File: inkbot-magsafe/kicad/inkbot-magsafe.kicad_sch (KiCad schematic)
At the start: 49 parts, among them J1 Panel FPC, U1 nRF52833-QDAA, U3 TPS22810DRV, U4 MIC5504-3.3, U5 BQ51050BRHL, Y1 32.768kHz, Y2 32MHz

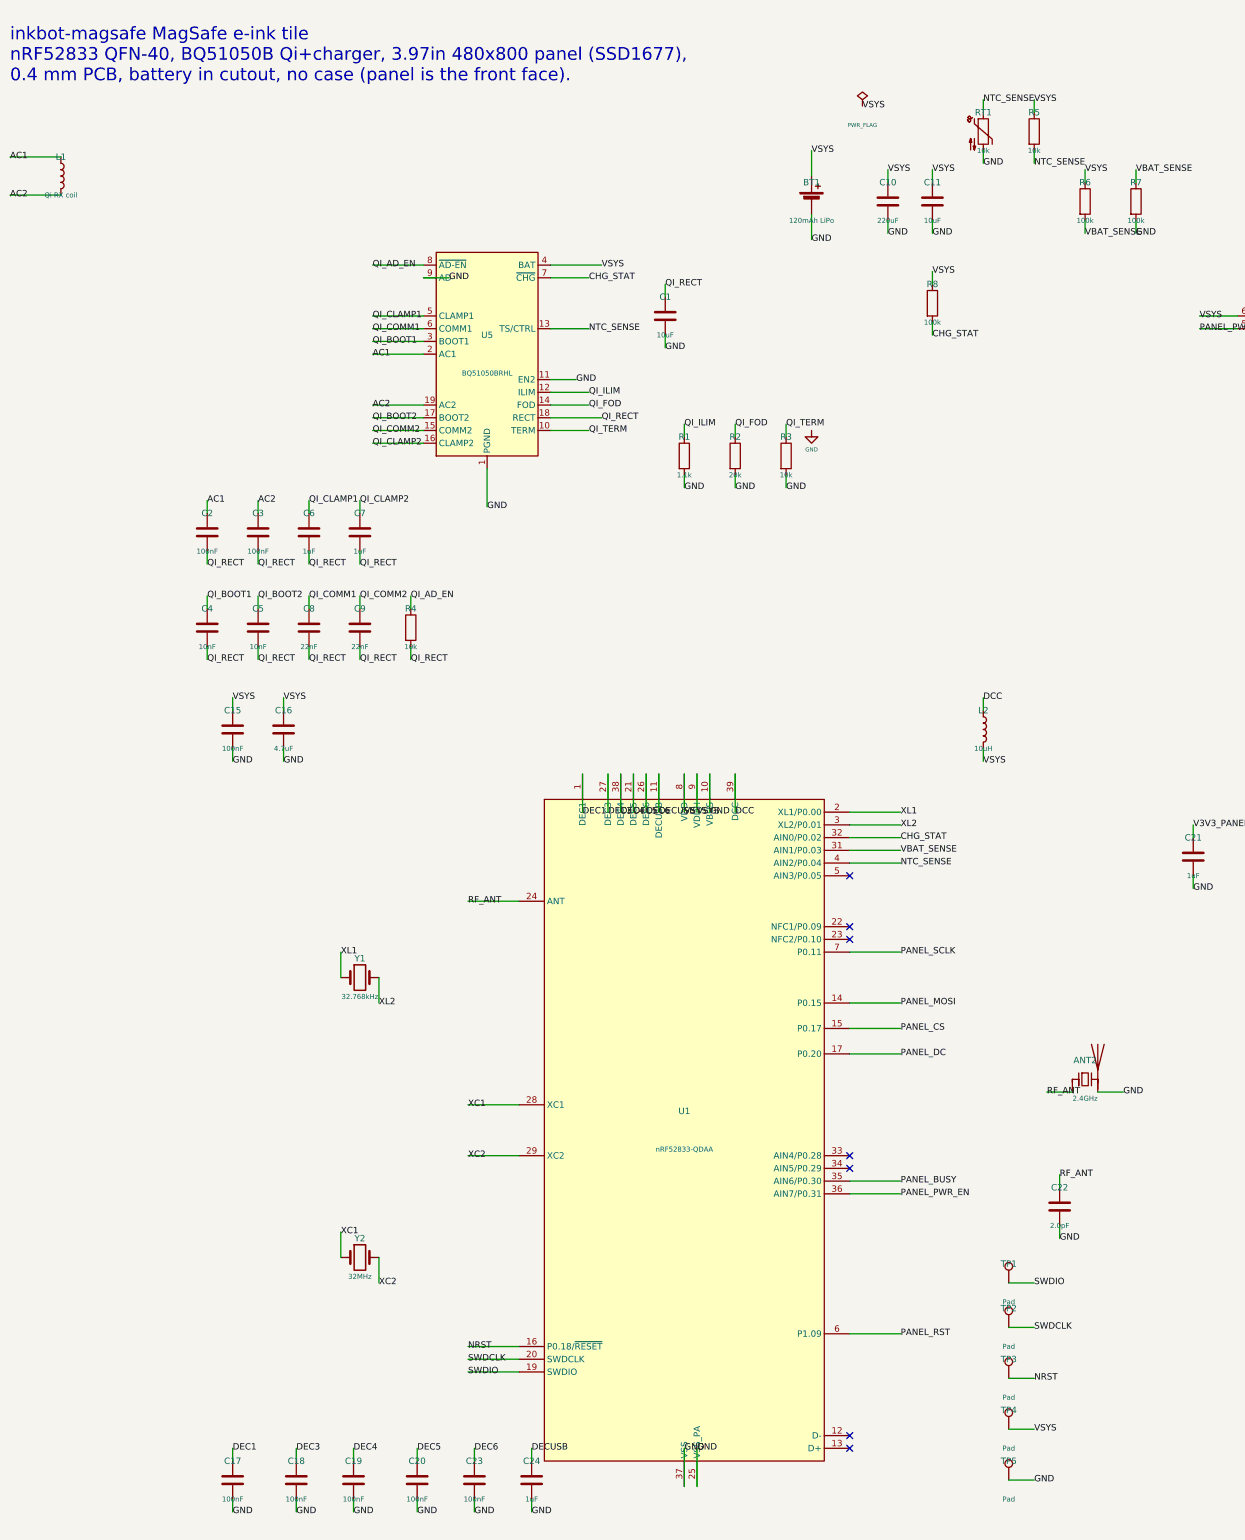
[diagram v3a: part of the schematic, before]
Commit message: inkbot-magsafe: switch to pre-certified Raytac MDBT50Q-512K module
Replace the bare nRF52833 QFN with the Raytac MDBT50Q-512K module (same
nRF52833 core, so firmware/memory are unchanged). The module integrates
the 2.4 GHz antenna, 32 MHz crystal, DC/DC, and RF match and carries
modular FCC/IC/CE/MIC/KC/SRRC approval, so the board drops the discrete
antenna, matching network, HFXO crystal, and DEC decoupling — deleting
the whole radio-layout and intentional-radiator-cert problem for ~1 mm
of added thickness (accepted).

Schematic regenerated on the module footprint (RF_Module:Raytac_MDBT50Q),
pins mapped by module pin number, netlist verified. Prototype board bumped
to 0.8 mm 4-layer. BOM, thickness table (~3.05 mm at the module), COGS
(~$34), pinmap, netlist, stackup, and design rationale updated.

Co-authored-by: Jason Hall <imjasonh@users.noreply.github.com>
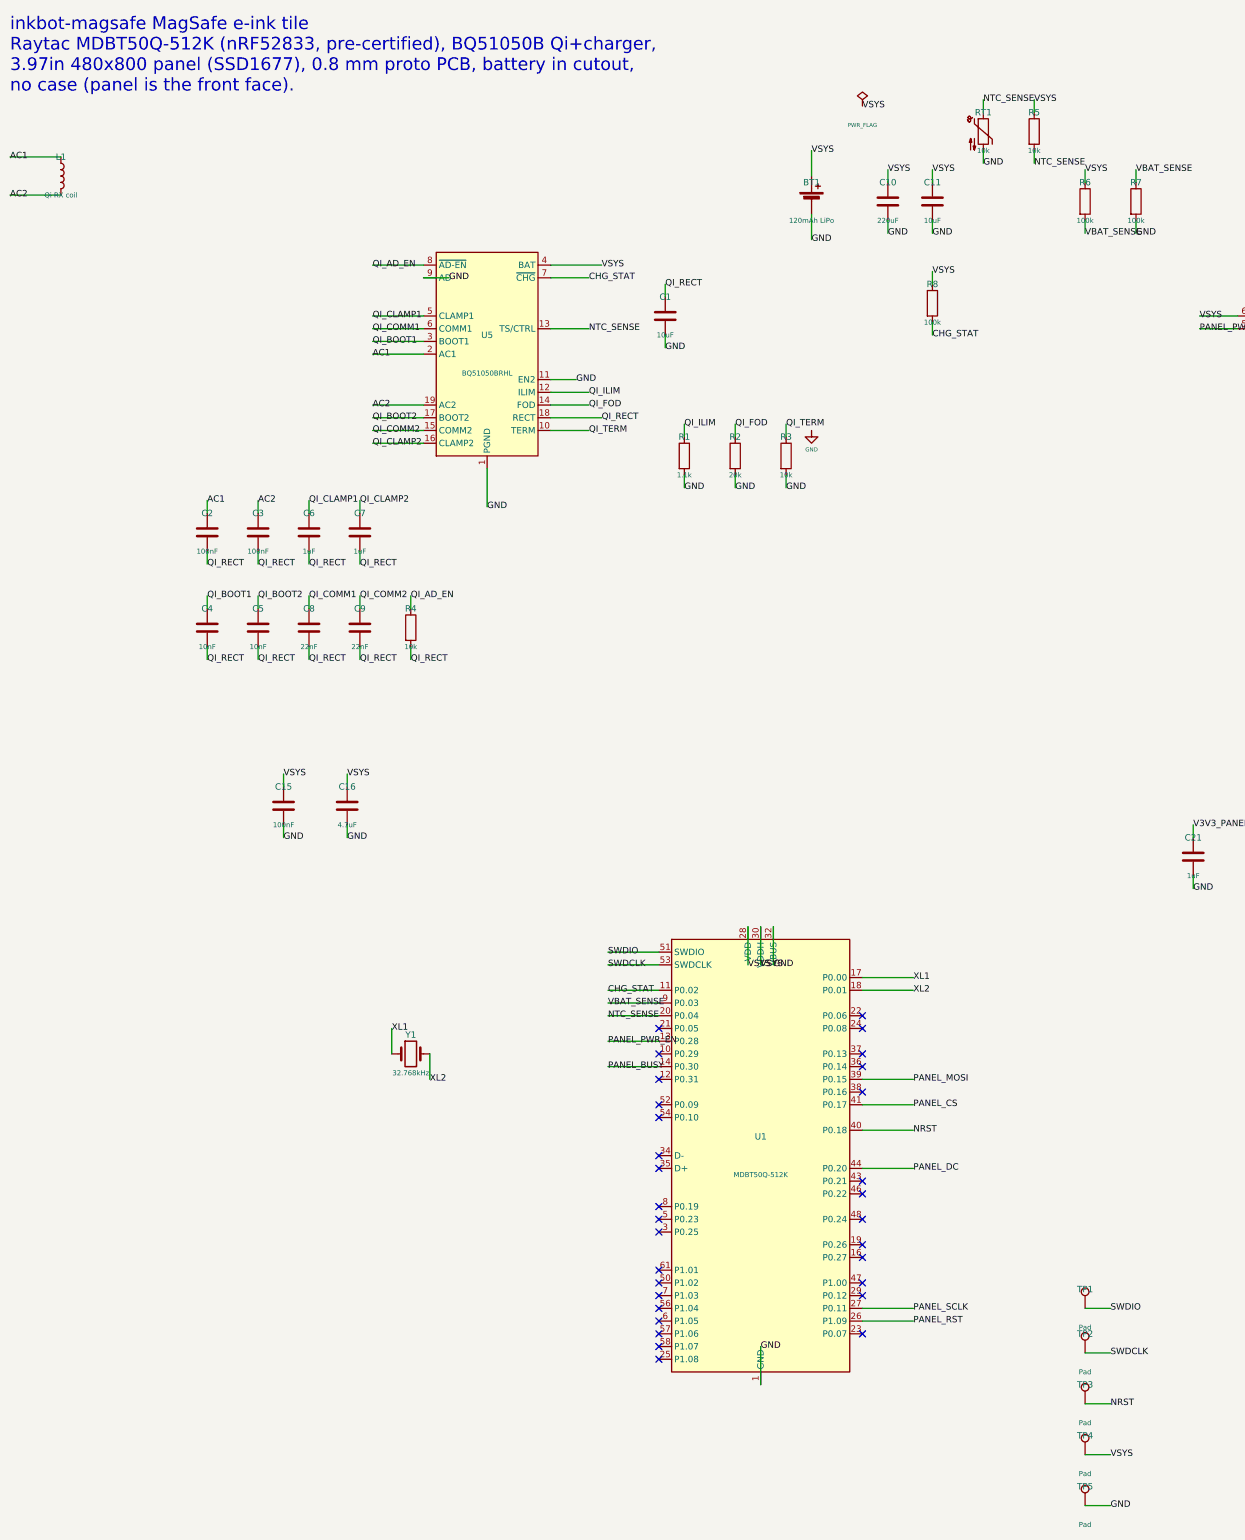
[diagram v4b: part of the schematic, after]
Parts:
- removed ANT2: 2.4GHz, Antenna_SMD:Antenna_Abracon_ACA-107-T, symbol Device:Antenna_Chip
- removed C17, C18, C19, C20, C23: 100nF, Capacitor_SMD:C_0402_1005Metric, symbol Device:C
- removed C22: 2.0pF, Capacitor_SMD:C_0402_1005Metric, symbol Device:C
- removed C24: 1uF, Capacitor_SMD:C_0402_1005Metric, symbol Device:C
- removed L2: 10uH, Inductor_SMD:L_0805_2012Metric, symbol Device:L
- removed U1: nRF52833-QDAA, Package_DFN_QFN:Nordic_QFN-40-1EP_5x5mm_P0.4mm, symbol MCU_Nordic:nRF52833_QDxx
- removed Y2: 32MHz, Crystal:Crystal_SMD_2012-2Pin_2.0x1.2mm, symbol Device:Crystal
- added U1: MDBT50Q-512K, RF_Module:Raytac_MDBT50Q, symbol RF_Module:MDBT50Q-512K
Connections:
- net CHG_STAT: now also U1.11 (P0.02)
- net GND: now also U1.1 (GND), U1.15 (GND), U1.2 (GND), U1.32 (VBUS), U1.33 (GND), U1.55 (GND)
- net NRST: now also U1.40 (P0.18)
- net NTC_SENSE: now also U1.20 (P0.04)
- net PANEL_BUSY: now also U1.14 (P0.30)
- net PANEL_CS: now also U1.41 (P0.17)
- net PANEL_DC: now also U1.44 (P0.20)
- net PANEL_MOSI: now also U1.39 (P0.15)
- net PANEL_PWR_EN: now also U1.13 (P0.28)
- net PANEL_RST: now also U1.26 (P1.09)
- net PANEL_SCLK: now also U1.27 (P0.11)
- net SWDCLK: now also U1.53 (SWDCLK)
- net SWDIO: now also U1.51 (SWDIO)
- net VBAT_SENSE: now also U1.9 (P0.03)
- net VSYS: now also U1.28 (VDD), U1.30 (VDDH)
- net XL1: now also U1.17 (P0.00)
- net XL2: now also U1.18 (P0.01)
- no-connect marks 7 -> 31
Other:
- note added: "inkbot-magsafe MagSafe e-ink tile Raytac MDBT50Q-512K (nRF52833, pre-certified), BQ51050B Qi+charger, 3.97in 480x800 panel (SSD1677), 0.8 mm proto PCB, battery in cutout, no case (panel is the front face)."
- note removed: "inkbot-magsafe MagSafe e-ink tile nRF52833 QFN-40, BQ51050B Qi+charger, 3.97in 480x800 panel (SSD1677), 0.4 mm PCB, battery in cutout, no case (panel is the front face)."

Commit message: inkbot-magsafe: regenerate the corrected electrical design
Co-authored-by: Jason Hall <imjasonh@users.noreply.github.com>
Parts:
- removed U3: TPS22810DRV, Package_TO_SOT_SMD:SOT-23-6, symbol Power_Management:TPS22810DRV
- removed U4: MIC5504-3.3, Package_TO_SOT_SMD:SOT-23-5, symbol Regulator_Linear:MIC5504-3.3YM5
- removed U5: BQ51050BRHL, Package_DFN_QFN:Texas_VQFN-RHL-20, symbol Battery_Management:BQ51050BRHL
- added C17, C19, C26, C29: 1uF 10V, Capacitor_SMD:C_0603_1608Metric, symbol Device:C
- added C18: 10uF 10V, Capacitor_SMD:C_0805_2012Metric, symbol Device:C
- added C20: 4.7nF, Capacitor_SMD:C_0603_1608Metric, symbol Device:C
- added C22: 4.7uF 10V, Capacitor_SMD:C_0603_1608Metric, symbol Device:C
- added C23, C24: 21pF C0G, Capacitor_SMD:C_0603_1608Metric, symbol Device:C
- added C25: 10nF, Capacitor_SMD:C_0603_1608Metric, symbol Device:C
- added C27, C28: 4.7uF 10V, Capacitor_SMD:C_0805_2012Metric, symbol Device:C
- added C30: 1uF 6.3V, Capacitor_SMD:C_0603_1608Metric, symbol Device:C
- added C31, C32, C33, C34, C35, C37: 4.7uF 25V, Capacitor_SMD:C_0805_2012Metric, symbol Device:C
- added C36: 1uF 50V, Capacitor_SMD:C_0603_1608Metric, symbol Device:C
- added D1, D2, D3: MBR0530, Diode_SMD:D_SOD-123, symbol Device:D
- added J2: Protected battery + NTC, Connector_Molex:Molex_Pico-EZmate_78171-0003_1x03-1MP_P1.20mm_Vertical, symbol Connector_Generic:Conn_01x03
- added J3: WR222230-26M8-G coil, Connector_Wire:SolderWire-0.5sqmm_1x02_P4.8mm_D0.9mm_OD2.3mm_Relief2x, symbol Connector_Generic:Conn_01x02
- added L2: WR222230-26M8-G 27uH, symbol Device:L
- added Q1: Si1308EDL-T1-GE3, Package_TO_SOT_SMD:SOT-323_SC-70, symbol Device:Q_NMOS_GSD
- added R10: 330k 1%, Resistor_SMD:R_0603_1608Metric, symbol Device:R
- added R11: 2.2R 1%, Resistor_SMD:R_0603_1608Metric, symbol Device:R
- added R12, R13, R14: 1M, Resistor_SMD:R_0603_1608Metric, symbol Device:R
- added R9: 1M 1%, Resistor_SMD:R_0603_1608Metric, symbol Device:R
- added RT2: 10k 3435K coil NTC, Resistor_SMD:R_0402_1005Metric, symbol Device:Thermistor_NTC
- added TP6: SYS, TestPoint:TestPoint_Pad_D1.0mm, symbol Connector:TestPoint
- added TP7: BAT, TestPoint:TestPoint_Pad_D1.0mm, symbol Connector:TestPoint
- added TP8: QI_OUT, TestPoint:TestPoint_Pad_D1.0mm, symbol Connector:TestPoint
- added TP9: PANEL_3V0, TestPoint:TestPoint_Pad_D1.0mm, symbol Connector:TestPoint
- added U2: BQ51013C, Package_DFN_QFN:Texas_VQFN-RHL-20, symbol inkbot_magsafe:BQ51013C
- added U3: BQ25185DLHR, inkbot_magsafe:BQ25185_DLH0010A, symbol inkbot_magsafe:BQ25185
- added U4: TPS7A2030PDBVR, Package_TO_SOT_SMD:SOT-23-5, symbol inkbot_magsafe:TPS7A2030P
- BT1: value 120mAh LiPo -> LP252030 100mAh protected
- C1: value 10uF -> 33nF 50V
- C10: value 220uF -> 22nF 50V; footprint Capacitor_SMD:C_1206_3216Metric -> Capacitor_SMD:C_0603_1608Metric
- C11: value 10uF -> 22nF 50V
- C12: value 1nF -> 10uF 25V; footprint Capacitor_SMD:C_0402_1005Metric -> Capacitor_SMD:C_0805_2012Metric
- C13: value 1uF -> 10uF 25V; footprint Capacitor_SMD:C_0402_1005Metric -> Capacitor_SMD:C_0805_2012Metric
- C14: value 1uF -> 100nF 50V; footprint Capacitor_SMD:C_0402_1005Metric -> Capacitor_SMD:C_0603_1608Metric
- C15: value 100nF -> 10uF 10V; footprint Capacitor_SMD:C_0402_1005Metric -> Capacitor_SMD:C_0805_2012Metric
- C16: value 4.7uF -> 100nF 10V
- C2: value 100nF -> 33nF 50V; footprint Capacitor_SMD:C_0402_1005Metric -> Capacitor_SMD:C_0603_1608Metric
- C21: value 1uF -> 4.7uF 10V
- C3: value 100nF -> 15nF 50V; footprint Capacitor_SMD:C_0402_1005Metric -> Capacitor_SMD:C_0603_1608Metric
- C4: value 10nF -> 820pF C0G 50V; footprint Capacitor_SMD:C_0402_1005Metric -> Capacitor_SMD:C_0603_1608Metric
- C5: value 10nF -> 130pF C0G 50V; footprint Capacitor_SMD:C_0402_1005Metric -> Capacitor_SMD:C_0603_1608Metric
- C6, C7: value 1uF -> 10nF 50V; footprint Capacitor_SMD:C_0402_1005Metric -> Capacitor_SMD:C_0603_1608Metric
- C8, C9: value 22nF -> 470nF 25V; footprint Capacitor_SMD:C_0402_1005Metric -> Capacitor_SMD:C_0603_1608Metric
- J1: value Panel FPC -> GDEM0397T81P panel FPC
- L1: value Qi RX coil -> VLS252010CX-100M-1 10uH; footprint Inductor_SMD:L_1210_3225Metric -> Inductor_SMD:L_TDK_NLV25_2.5x2.0mm
- R1: value 1.1k -> 845R 1%; footprint Resistor_SMD:R_0402_1005Metric -> Resistor_SMD:R_0603_1608Metric
- R2: value 20k -> 200R 1%; footprint Resistor_SMD:R_0402_1005Metric -> Resistor_SMD:R_0603_1608Metric
- R3: value 10k -> 20k 1%; footprint Resistor_SMD:R_0402_1005Metric -> Resistor_SMD:R_0603_1608Metric
- R4: value 10k -> DNP; footprint Resistor_SMD:R_0402_1005Metric -> Resistor_SMD:R_0603_1608Metric
- R5: value 10k -> 100k; footprint Resistor_SMD:R_0402_1005Metric -> Resistor_SMD:R_0603_1608Metric
- R6: value 100k -> 24k 1%; footprint Resistor_SMD:R_0402_1005Metric -> Resistor_SMD:R_0603_1608Metric
- R7: value 100k -> 7.5k 1%; footprint Resistor_SMD:R_0402_1005Metric -> Resistor_SMD:R_0603_1608Metric
- R8: value 100k -> 2k; footprint Resistor_SMD:R_0402_1005Metric -> Resistor_SMD:R_0603_1608Metric
- RT1: value 10k -> 10k 3435K bonded to cell; footprint Resistor_SMD:R_0402_1005Metric -> (none)
- TP1: value Pad -> SWDIO; footprint TestPoint:TestPoint_Pad_D1.5mm -> TestPoint:TestPoint_Pad_D1.0mm
- TP2: value Pad -> SWDCLK; footprint TestPoint:TestPoint_Pad_D1.5mm -> TestPoint:TestPoint_Pad_D1.0mm
- TP3: value Pad -> NRST; footprint TestPoint:TestPoint_Pad_D1.5mm -> TestPoint:TestPoint_Pad_D1.0mm
- TP4: value Pad -> VDD_NRF; footprint TestPoint:TestPoint_Pad_D1.5mm -> TestPoint:TestPoint_Pad_D1.0mm
- TP5: value Pad -> GND; footprint TestPoint:TestPoint_Pad_D1.5mm -> TestPoint:TestPoint_Pad_D1.0mm
- Y1: value 32.768kHz -> FC-135 32.768kHz 12.5pF; footprint Crystal:Crystal_SMD_2012-2Pin_2.0x1.2mm -> Crystal:Crystal_SMD_3215-2Pin_3.2x1.5mm
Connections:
- net PANEL_CT is gone; now on net QI_RECT: C12.1
- net QI_TERM is gone; now on net QI_RECT: R3.1
- net VSW_PANEL is gone; now on net QI_RECT: C13.1
- net PANEL_BUSY: now also J1.9 (Pin_9); no longer J1.5 (Pin_5)
- net PANEL_CS: now also J1.12 (Pin_12); no longer J1.8 (Pin_8)
- net PANEL_DC: now also J1.11 (Pin_11); no longer J1.7 (Pin_7)
- net PANEL_MOSI: now also J1.14 (Pin_14); no longer J1.10 (Pin_10)
- net PANEL_PWR_EN: now also U1.12 (P0.31), U4.3 (EN); no longer U1.13 (P0.28)
- net PANEL_RST: now also J1.10 (Pin_10); no longer J1.6 (Pin_6)
- net PANEL_SCLK: now also J1.13 (Pin_13); no longer J1.9 (Pin_9)
- net QI_BOOT1: now also C6.1, U2.3 (BOOT1); no longer C4.1
- net QI_BOOT2: now also C7.1, U2.17 (BOOT2); no longer C5.1
- net QI_CLAMP1: now also C8.1, U2.5 (CLAMP1); no longer C6.1
- net QI_CLAMP2: now also C9.1, U2.16 (CLAMP2); no longer C7.1
- net QI_COMM1: now also C10.1, U2.6 (COMM1); no longer C8.1
- net QI_COMM2: now also C11.1, U2.15 (COMM2); no longer C9.1
- net QI_FOD: now also R1.2, R3.2, R4.2, U2.14 (FOD)
- net QI_ILIM: now also U2.12 (ILIM)
- net QI_RECT: now also C14.1, U2.18 (RECT); no longer C1.1, C2.2, C3.2, C4.2, C5.2, C6.2, C7.2, C8.2, C9.2, R4.2
- net VBAT_SENSE: now also C25.1, R10.1, R9.2; no longer R6.2, R7.1
- net XL1: now also C23.1
- net XL2: now also C24.1
- net CHG_STAT2: now reaches U1.21 (P0.05)
- net CHG_STAT2: now also U3.3 (STAT2)
- net CHG_EN_N: now reaches U1.22 (P0.06)
- net CHG_EN_N: now also R5.1, U3.4 (~{CE})
- net PANEL_3V0: now reaches J1.15 (Pin_15)
- net PANEL_3V0: now also J1.16 (Pin_16), L1.1, C27.1, C28.1, C29.1, TP9.1, U4.5 (OUT)
- net EP: now reaches J1.17 (Pin_17)
- net EP: now also BT1.2 (-), C12.2, C13.2, C14.2, C15.2, C16.2, C21.2, J1.8 (Pin_8), R2.2, R5.2, R6.2, R7.2, RT1.2, TP5.1, U1.1 (GND), U1.15 (GND), U1.2 (GND), U1.33 (GND), U1.55 (GND), C17.2, C18.2, C19.2, C20.2, C22.2, C23.2, C24.2, C25.2, C26.2, C27.2, C28.2, C29.2, C30.2, C31.2, C32.2, C33.2, C34.2, C35.2, C36.2, D2.1 (K), J2.3 (Pin_3), R10.2, R11.2, R12.2, R13.2, R14.2, RT2.2, U2.1 (PGND), U2.10 (EN1), U2.11 (EN2), U2.20 (PGND), U2.21 (EP), U2.9 (AD), U3.11 (EP), U3.5 (GND), U4.2 (GND)
- net PANEL_VDD: now reaches J1.18 (Pin_18)
- net PANEL_VDD: now also C30.1
- net PANEL_VSH1: now reaches J1.20 (Pin_20)
- net PANEL_VSH1: now also C32.1
- net PANEL_VGH: now reaches J1.21 (Pin_21)
- net PANEL_VGH: now also C33.1, D3.1 (K), R13.1
- net PANEL_VSL: now reaches J1.22 (Pin_22)
- net PANEL_VSL: now also C34.1
- net PANEL_VGL: now reaches J1.23 (Pin_23)
- net PANEL_VGL: now also C35.1, D1.2 (A), R14.1
- net PANEL_VCOM: now reaches J1.24 (Pin_24)
- net PANEL_VCOM: now also C36.1
- net AC1 renamed QI_COIL_A
- net QI_COIL_A: now also C1.1, C3.1, J3.1 (Pin_1), L2.1; no longer L1.1
- net AC2 renamed PANEL_SW
- net PANEL_SW: now also C37.1, D3.2 (A), Q1.3 (D); no longer C3.1
- net CHG_STAT renamed CHG_ISET_COMP
- net CHG_ISET_COMP: now also C20.1; no longer U1.11 (P0.02)
- removed net GND: BT1.2 (-), C1.2, C10.2, C11.2, C12.2, C13.2, C14.2, C15.2, C16.2, C21.2, J1.3 (Pin_3), J1.4 (Pin_4), R1.2, R2.2, R3.2, R7.2, RT1.2, TP5.1, U1.1 (GND), U1.15 (GND), U1.2 (GND), U1.32 (VBUS), U1.33 (GND), U1.55 (GND)
- removed net NTC_SENSE: R5.2, RT1.1, U1.20 (P0.04)
- net QI_AD_EN renamed QI_OUT
- net QI_OUT: now also C15.1, C16.1, C17.1, TP8.1, U2.4 (OUT), U3.10 (IN)
- removed net V3V3_PANEL: C14.1, C21.1, J1.1 (Pin_1), J1.2 (Pin_2)
- removed net VSYS: BT1.1 (+), C10.1, C11.1, C15.1, C16.1, R5.1, R6.1, R8.1, TP4.1, U1.28 (VDD), U1.30 (VDDH)
- new net BAT: BT1.1 (+), C19.1, J2.1 (Pin_1), R9.1, TP7.1, U3.2 (BAT)
- new net BAT_NTC: J2.2 (Pin_2), RT1.1, U3.6 (TS/MR)
- new net CHG_ISET: R7.1, R8.1, U3.8 (ISET)
- new net CHG_STAT1: U1.20 (P0.04), U3.9 (STAT1)
- new net CHG_VSET: R6.1, U3.7 (ILIM/VSET)
- new net PANEL_GDR: J1.2 (Pin_2), Q1.1 (G), R12.1
- new net PANEL_PUMP: C37.2, D1.1 (K), D2.2 (A)
- new net PANEL_RESE: J1.3 (Pin_3), Q1.2 (S), R11.1
- new net PANEL_VSH2: C31.1, J1.5 (Pin_5)
- new net QI_AC1: C1.2, C10.2, C2.2, C3.2, C4.1, C5.1, C6.2, C8.2, U2.2 (AC1)
- new net QI_AC2: C11.2, C4.2, C5.2, C7.2, C9.2, J3.2 (Pin_2), L2.2, U2.19 (AC2)
- new net QI_COIL_NTC: RT2.1, U2.13 (TS/CTRL)
- new net QI_PRESENT: U1.11 (P0.02), U2.7 (CHG)
- new net SYS: C18.1, C21.1, C26.1, TP6.1, U1.30 (VDDH), U3.1 (SYS), U4.1 (IN)
- new net VDD_NRF: C22.1, TP4.1, U1.28 (VDD)
- no-connect marks 31 -> 48
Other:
- note added: "inkbot-magsafe EVT schematic BQ51013C Qi 1.3 receiver + BQ25185 40 mA protected-cell charger, Raytac MDBT50Q-512K in VDDH mode, and the complete GDEM0397T81P SSD1677 boost circuit. Qi resonance and FOD values require EVT tuning."
- note removed: "inkbot-magsafe MagSafe e-ink tile Raytac MDBT50Q-512K (nRF52833, pre-certified), BQ51050B Qi+charger, 3.97in 480x800 panel (SSD1677), 0.8 mm proto PCB, battery in cutout, no case (panel is the front face)."

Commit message: inkbot-magsafe: update the coil connector netlist
Co-authored-by: Jason Hall <imjasonh@users.noreply.github.com>
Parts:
- J3: footprint Connector_Wire:SolderWire-0.5sqmm_1x02_P4.8mm_D0.9mm_OD2.3mm_Relief2x -> inkbot_magsafe:Coil_SolderPads

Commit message: inkbot-magsafe: harden the EVT hardware design
Co-authored-by: Jason Hall <imjasonh@users.noreply.github.com>
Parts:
- removed C25: 10nF, Capacitor_SMD:C_0603_1608Metric, symbol Device:C
- removed R10: 330k 1%, Resistor_SMD:R_0603_1608Metric, symbol Device:R
- removed R13, R14: 1M, Resistor_SMD:R_0603_1608Metric, symbol Device:R
- removed R9: 1M 1%, Resistor_SMD:R_0603_1608Metric, symbol Device:R
- added C38: 220uF 6.3V X5R, Capacitor_SMD:C_1206_3216Metric, symbol Device:C
- C1, C2, C3: footprint Capacitor_SMD:C_0603_1608Metric -> Capacitor_SMD:C_0805_2012Metric
- C12, C13: footprint Capacitor_SMD:C_0805_2012Metric -> Capacitor_SMD:C_1206_3216Metric
- C15: value 10uF 10V -> 10uF 25V; footprint Capacitor_SMD:C_0805_2012Metric -> Capacitor_SMD:C_1206_3216Metric
- C17, C29: value 1uF 10V -> 1uF 25V
- C18: value 10uF 10V -> 10uF 25V
- C23, C24: value 21pF C0G -> 22pF C0G
- C28: value 4.7uF 10V -> 4.7uF 25V
- C30: value 1uF 6.3V -> 1uF 50V
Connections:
- net EP: now also C38.2
- net SYS: now also C38.1
- net VBAT_SENSE: no longer names the net of U1.9 (P0.03)
- no-connect marks 48 -> 49

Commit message: inkbot-magsafe: bound panel inrush and sense coil heat
Co-authored-by: Jason Hall <imjasonh@users.noreply.github.com>
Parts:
- C1, C2: value 33nF 50V -> 33nF C0G 50V
- C27: value 4.7uF 10V -> 100uF 6.3V X5R; footprint Capacitor_SMD:C_0805_2012Metric -> Capacitor_SMD:C_1206_3216Metric
- C3: value 15nF 50V -> 15nF C0G 50V
- C38: value 220uF 6.3V X5R -> 47uF 10V X5R
- J3: value WR222230-26M8-G coil -> WR222230 coil + bonded NTC; symbol Connector_Generic:Conn_01x02 -> Connector_Generic:Conn_01x04
- RT2: footprint Resistor_SMD:R_0402_1005Metric -> (none)
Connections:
- net EP: now also J3.4 (Pin_4)
- net QI_COIL_NTC: now also J3.3 (Pin_3)
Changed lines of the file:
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@@
     )
   )
-  (symbol (lib_id "Connector_Generic:Conn_01x02") (at 25.40 44.45 0)
+  (symbol (lib_id "Connector_Generic:Conn_01x04") (at 25.40 44.45 0)
     (property "Reference" "J3" (at 25.40 40.64 0)
       (effects (font (size 1.27 1.27))))
-    (property "Value" "WR222230-26M8-G coil" (at 25.40 48.26 0)
+    (property "Value" "WR222230 coil + bonded NTC" (at 25.40 48.26 0)
       (effects (font (size 1.0 1.0))))
     (property "Footprint" "inkbot_magsafe:Coil_SolderPads" (at 25.40 49.53 0)
@@
     (property "Reference" "C1" (at 41.91 66.04 0)
       (effects (font (size 1.27 1.27))))
-    (property "Value" "33nF 50V" (at 41.91 73.66 0)
+    (property "Value" "33nF C0G 50V" (at 41.91 73.66 0)
       (effects (font (size 1.0 1.0))))
     (property "Footprint" "Capacitor_SMD:C_0805_2012Metric" (at 41.91 74.93 0)
@@
     (property "Reference" "C2" (at 49.53 66.04 0)
       (effects (font (size 1.27 1.27))))
-    (property "Value" "33nF 50V" (at 49.53 73.66 0)
+    (property "Value" "33nF C0G 50V" (at 49.53 73.66 0)
       (effects (font (size 1.0 1.0))))
     (property "Footprint" "Capacitor_SMD:C_0805_2012Metric" (at 49.53 74.93 0)
@@
     (property "Reference" "C3" (at 58.42 66.04 0)
       (effects (font (size 1.27 1.27))))
-    (property "Value" "15nF 50V" (at 58.42 73.66 0)
+    (property "Value" "15nF C0G 50V" (at 58.42 73.66 0)
       (effects (font (size 1.0 1.0))))
     (property "Footprint" "Capacitor_SMD:C_0805_2012Metric" (at 58.42 74.93 0)
@@
     (property "Value" "10k 3435K coil NTC" (at 165.10 68.58 0)
       (effects (font (size 1.0 1.0))))
-    (property "Footprint" "Resistor_SMD:R_0402_1005Metric" (at 165.10 69.85 0)
+    (property "Footprint" "" (at 165.10 69.85 0)
       (effects (font (size 1.27 1.27)) hide))
     (property "LCSC" "" (at 165.10 71.12 0)
@@
     (property "Reference" "C38" (at 229.87 171.45 0)
       (effects (font (size 1.27 1.27))))
-    (property "Value" "220uF 6.3V X5R" (at 229.87 179.07 0)
+    (property "Value" "47uF 10V X5R" (at 229.87 179.07 0)
       (effects (font (size 1.0 1.0))))
     (property "Footprint" "Capacitor_SMD:C_1206_3216Metric" (at 229.87 180.34 0)
@@
     (property "Reference" "C27" (at 304.80 156.21 0)
       (effects (font (size 1.27 1.27))))
-    (property "Value" "4.7uF 10V" (at 304.80 163.83 0)
-      (effects (font (size 1.0 1.0))))
-    (property "Footprint" "Capacitor_SMD:C_0805_2012Metric" (at 304.80 165.10 0)
+    (property "Value" "100uF 6.3V X5R" (at 304.80 163.83 0)
+      (effects (font (size 1.0 1.0))))
+    (property "Footprint" "Capacitor_SMD:C_1206_3216Metric" (at 304.80 165.10 0)
       (effects (font (size 1.27 1.27)) hide))
     (property "LCSC" "" (at 304.80 166.37 0)
@@
     (stroke (width 0) (type default))
   )
+  (wire (pts (xy 20.32 41.91) (xy 12.70 41.91))
+    (stroke (width 0) (type default))
+  )
   (wire (pts (xy 20.32 44.45) (xy 12.70 44.45))
     (stroke (width 0) (type default))
@@
     (stroke (width 0) (type default))
   )
+  (wire (pts (xy 20.32 49.53) (xy 12.70 49.53))
+    (stroke (width 0) (type default))
+  )
   (wire (pts (xy 25.40 21.59) (xy 25.40 16.51))
     (stroke (width 0) (type default))
@@
     (effects (font (size 1.27 1.27)) (justify left))
   )
-  (label "QI_COIL_A" (at 12.70 44.45 0)
-    (effects (font (size 1.27 1.27)) (justify left))
-  )
-  (label "QI_AC2" (at 12.70 46.99 0)
-    (effects (font (size 1.27 1.27)) (justify left))
-  )
+  (label "QI_COIL_A" (at 12.70 41.91 0)
+    (effects (font (size 1.27 1.27)) (justify left))
+  )
+  (label "QI_AC2" (at 12.70 44.45 0)
+    (effects (font (size 1.27 1.27)) (justify left))
+  )
+  (label "QI_COIL_NTC" (at 12.70 46.99 0)
+    (effects (font (size 1.27 1.27)) (justify left))
+  )
+  (label "GND" (at 12.70 49.53 0)
+    (effects (font (size 1.27 1.27)) (justify left))
+  )
